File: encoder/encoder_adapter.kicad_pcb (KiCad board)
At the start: 2 copper layers, 24 x 17.5 mm, 10 parts, among them SW1 Rotary_Encoder_Switch, X1 Conn_01x04, X2 Conn_01x04

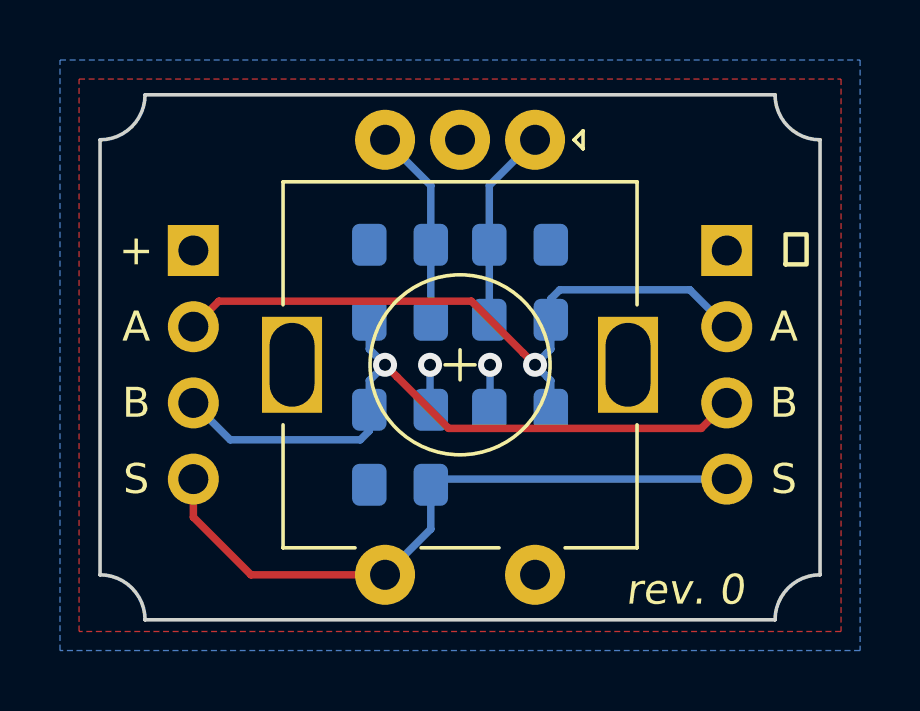
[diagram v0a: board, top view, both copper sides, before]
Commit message: fixed VCC not connecting to A
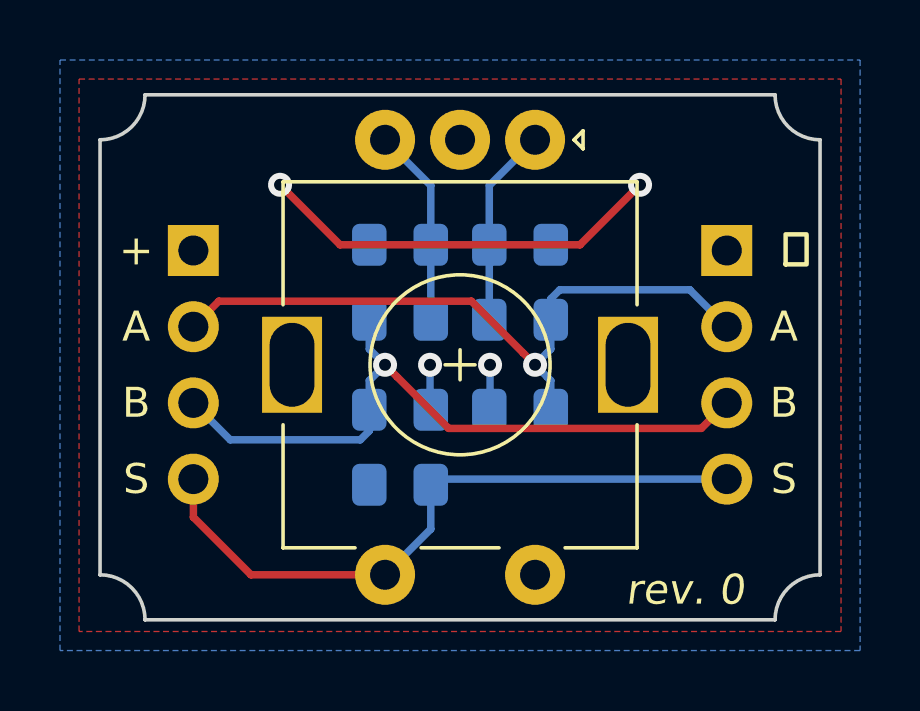
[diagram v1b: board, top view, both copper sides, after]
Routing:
- net VDD: track 0.00 -> 13.7 mm, vias 0 -> 2

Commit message: set revision to 1
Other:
- board text added: "rev. 1"
- board text removed: "rev. 0"
